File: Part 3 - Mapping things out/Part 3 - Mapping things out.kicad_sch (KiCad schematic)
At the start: 15 parts, among them J1 BUS 1, SW1 RESET, U1 74AHC14, U2 74AHC174

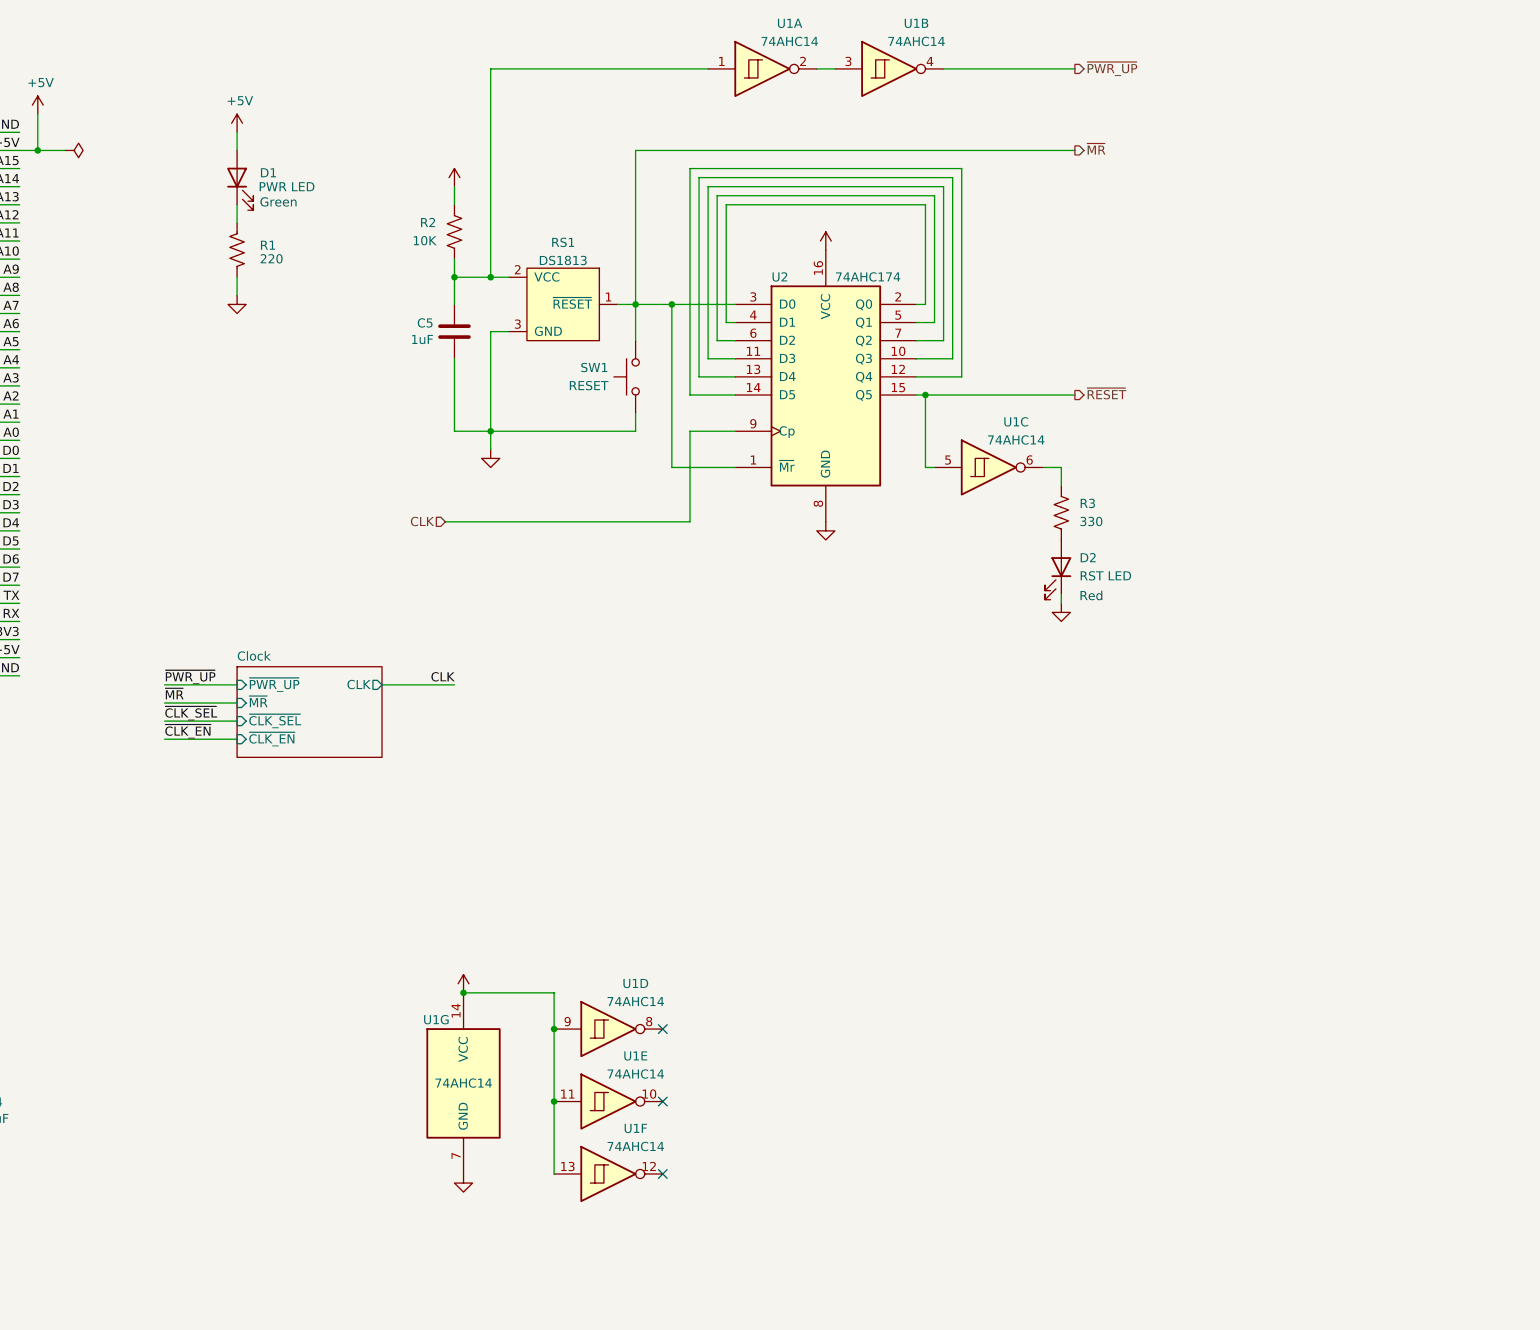
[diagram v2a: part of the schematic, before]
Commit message: Added software selectable speed control
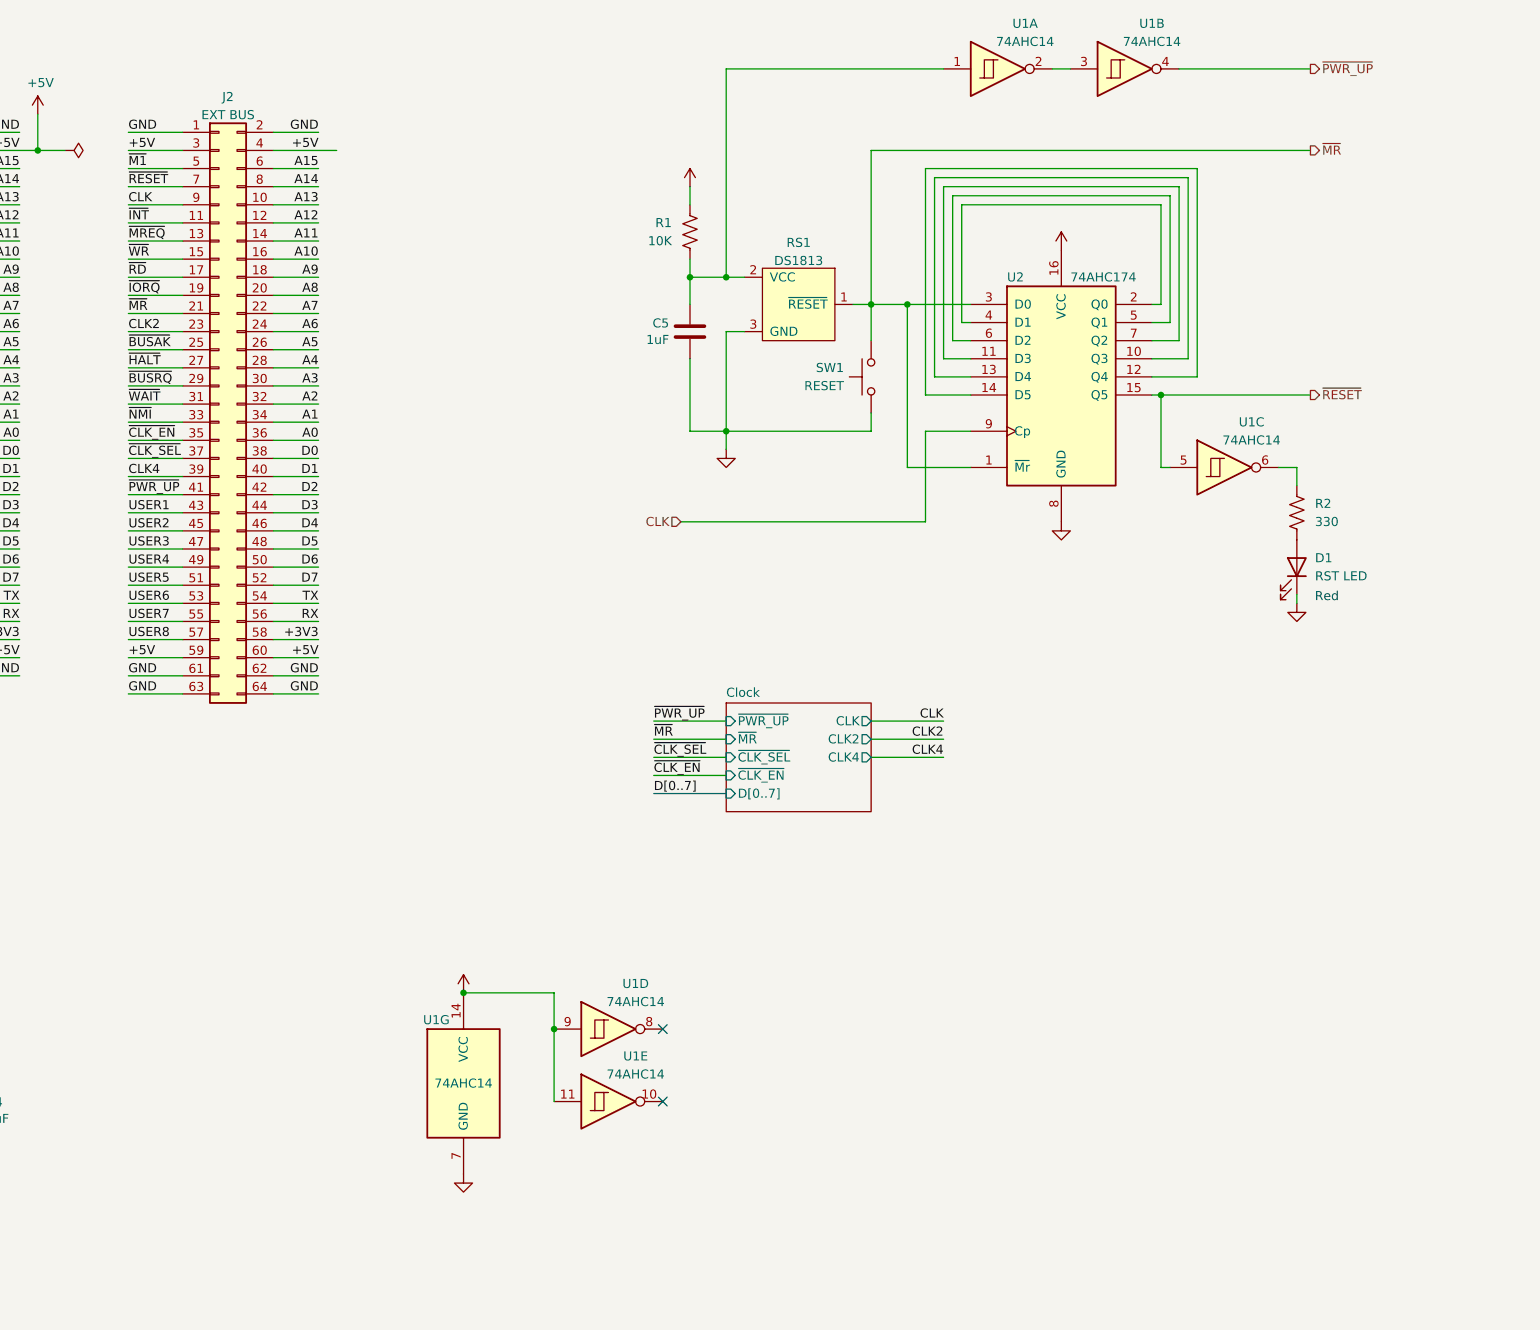
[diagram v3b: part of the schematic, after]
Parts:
- removed D1: PWR LED, LED_THT:LED_D3.0mm, symbol Device:LED
- removed R1: 220, Resistor_THT:R_Axial_DIN0207_L6.3mm_D2.5mm_P10.16mm_Horizontal, symbol Device:R_US
- removed unit 6 of U1
- added J2: EXT BUS, Connector_PinSocket_2.54mm:PinSocket_2x32_P2.54mm_Vertical, symbol Connector_Generic:Conn_02x32_Odd_Even
- SW1: footprint Button_Switch_THT:SW_PUSH-12mm_Wuerth-430476085716 -> Button_Switch_THT:SW_Tactile_SPST_Angled_PTS645Vx58-2LFS
- renumbered D2 to D1, R2 to R1, R3 to R2
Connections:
- net +3V3: now also J2.58 (Pin_58)
- net +5V: now also J2.3 (Pin_3), J2.4 (Pin_4), J2.59 (Pin_59), J2.60 (Pin_60)
- net A0: now also J2.36 (Pin_36)
- net A1: now also J2.34 (Pin_34)
- net A10: now also J2.16 (Pin_16)
- net A11: now also J2.14 (Pin_14)
- net A12: now also J2.12 (Pin_12)
- net A13: now also J2.10 (Pin_10)
- net A14: now also J2.8 (Pin_8)
- net A15: now also J2.6 (Pin_6)
- net A2: now also J2.32 (Pin_32)
- net A3: now also J2.30 (Pin_30)
- net A4: now also J2.28 (Pin_28)
- net A5: now also J2.26 (Pin_26)
- net A6: now also J2.24 (Pin_24)
- net A7: now also J2.22 (Pin_22)
- net A8: now also J2.20 (Pin_20)
- net A9: now also J2.18 (Pin_18)
- net CLK: now also J2.9 (Pin_9)
- net CLK2: now also J2.23 (Pin_23)
- net CLK4: now also J2.39 (Pin_39)
- net D0: now also J2.38 (Pin_38)
- net D1: now also J2.40 (Pin_40)
- net D2: now also J2.42 (Pin_42)
- net D3: now also J2.44 (Pin_44)
- net D4: now also J2.46 (Pin_46)
- net D5: now also J2.48 (Pin_48)
- net D6: now also J2.50 (Pin_50)
- net D7: now also J2.52 (Pin_52)
- net GND: now also J2.1 (Pin_1), J2.2 (Pin_2), J2.61 (Pin_61), J2.62 (Pin_62), J2.63 (Pin_63), J2.64 (Pin_64)
- net RX: now also J2.56 (Pin_56)
- net TX: now also J2.54 (Pin_54)
- net USER1: now also J2.43 (Pin_43)
- net USER2: now also J2.45 (Pin_45)
- net USER3: now also J2.47 (Pin_47)
- net USER4: now also J2.49 (Pin_49)
- net USER5: now also J2.51 (Pin_51)
- net USER6: now also J2.53 (Pin_53)
- net USER7: now also J2.55 (Pin_55)
- net USER8: now also J2.57 (Pin_57)
- net ~{BUSAK}: now also J2.25 (Pin_25)
- net ~{BUSRQ}: now also J2.29 (Pin_29)
- net ~{CLK_EN}: now also J2.35 (Pin_35)
- net ~{CLK_SEL}: now also J2.37 (Pin_37)
- net ~{HALT}: now also J2.27 (Pin_27)
- net ~{INT}: now also J2.11 (Pin_11)
- net ~{IORQ}: now also J2.19 (Pin_19)
- net ~{M1}: now also J2.5 (Pin_5)
- net ~{MREQ}: now also J2.13 (Pin_13)
- net ~{MR}: now also J2.21 (Pin_21)
- net ~{NMI}: now also J2.33 (Pin_33)
- net ~{PWR_UP}: now also J2.41 (Pin_41)
- net ~{RD}: now also J2.17 (Pin_17)
- net ~{RESET}: now also J2.7 (Pin_7)
- net ~{WAIT}: now also J2.31 (Pin_31)
- net ~{WR}: now also J2.15 (Pin_15)
- no-connect marks 3 -> 2
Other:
- sheet Clock ports: added CLK2, CLK4, D[0..7]; removed none
- note removed: "Green"
- company: Frédéric Segard -> Frédéric Segard, aka : Micro Hobbyist
- moved on the sheet: C5, D1, R1, R2, RS1, SW1, U1A, U1B, U1C, U2

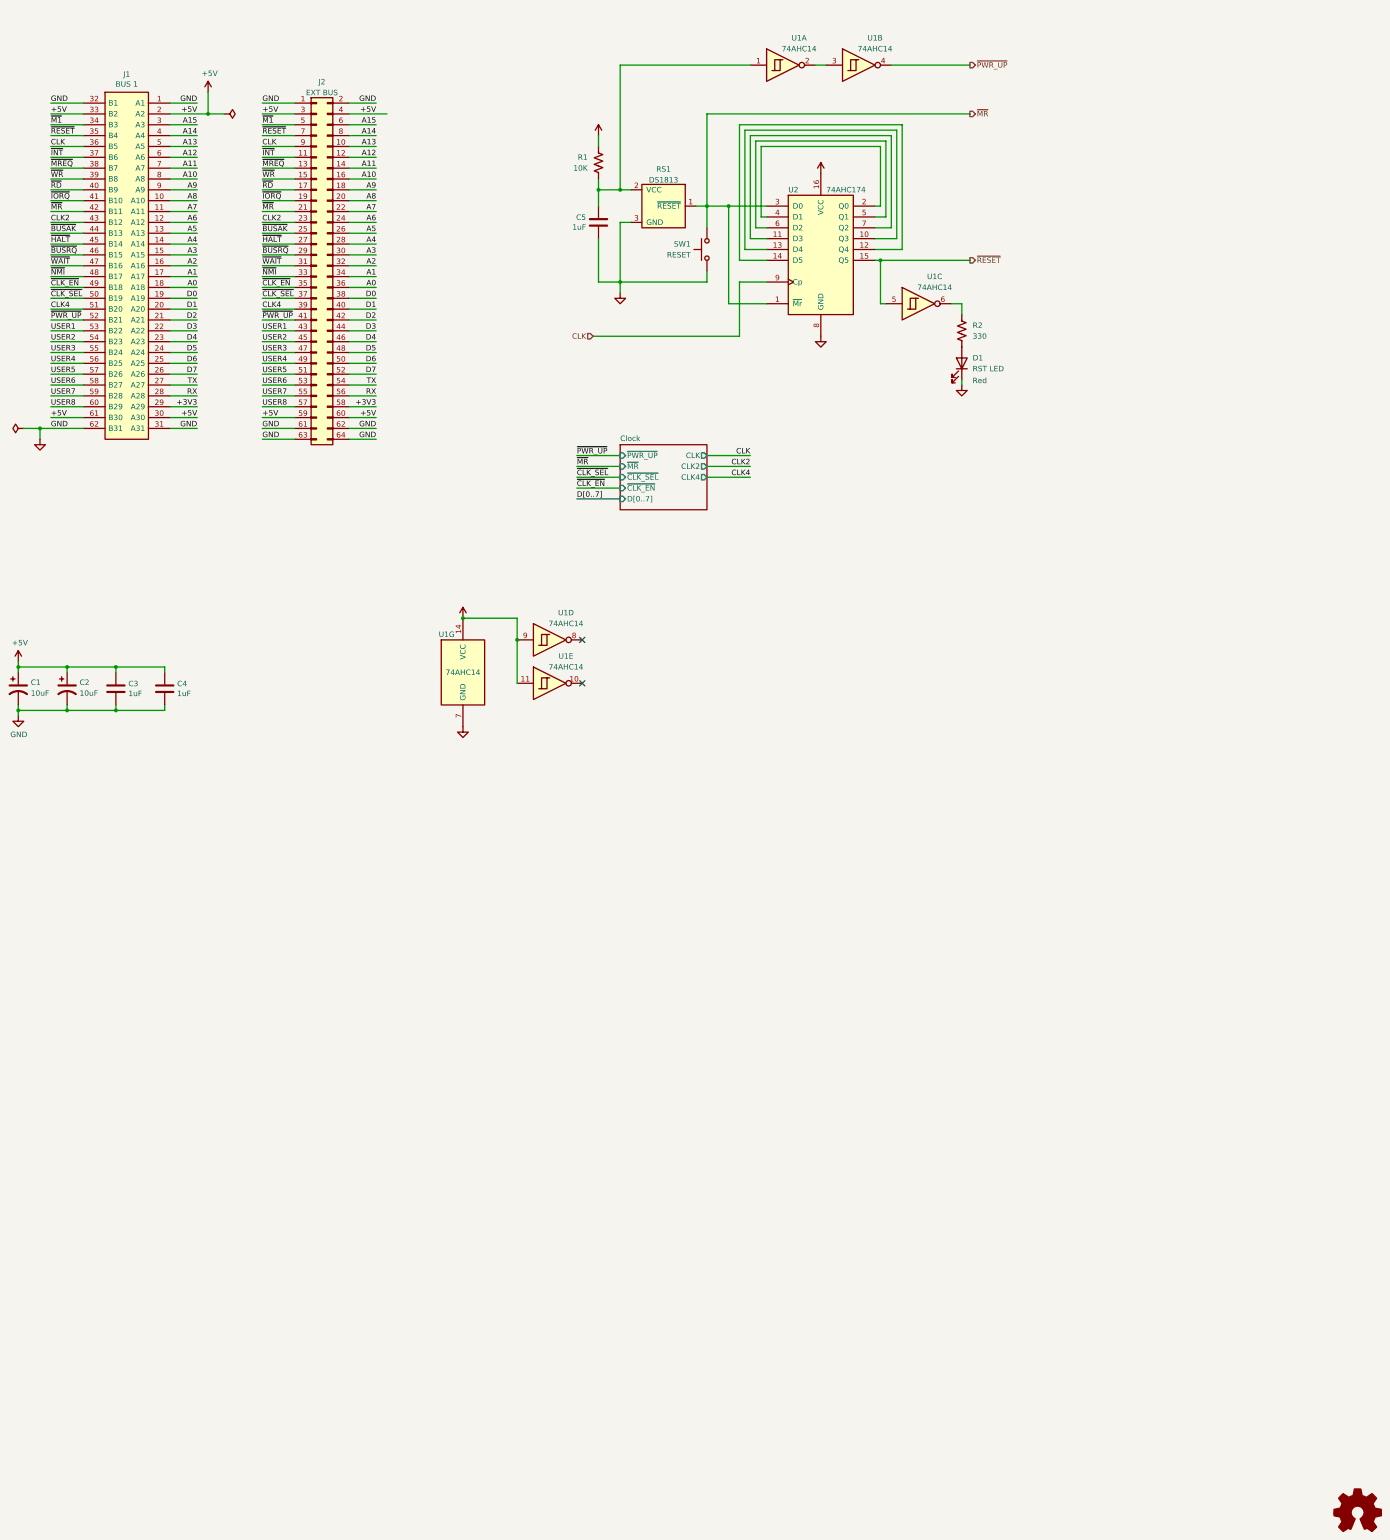
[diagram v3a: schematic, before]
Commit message: Updated clock, and created CPU card
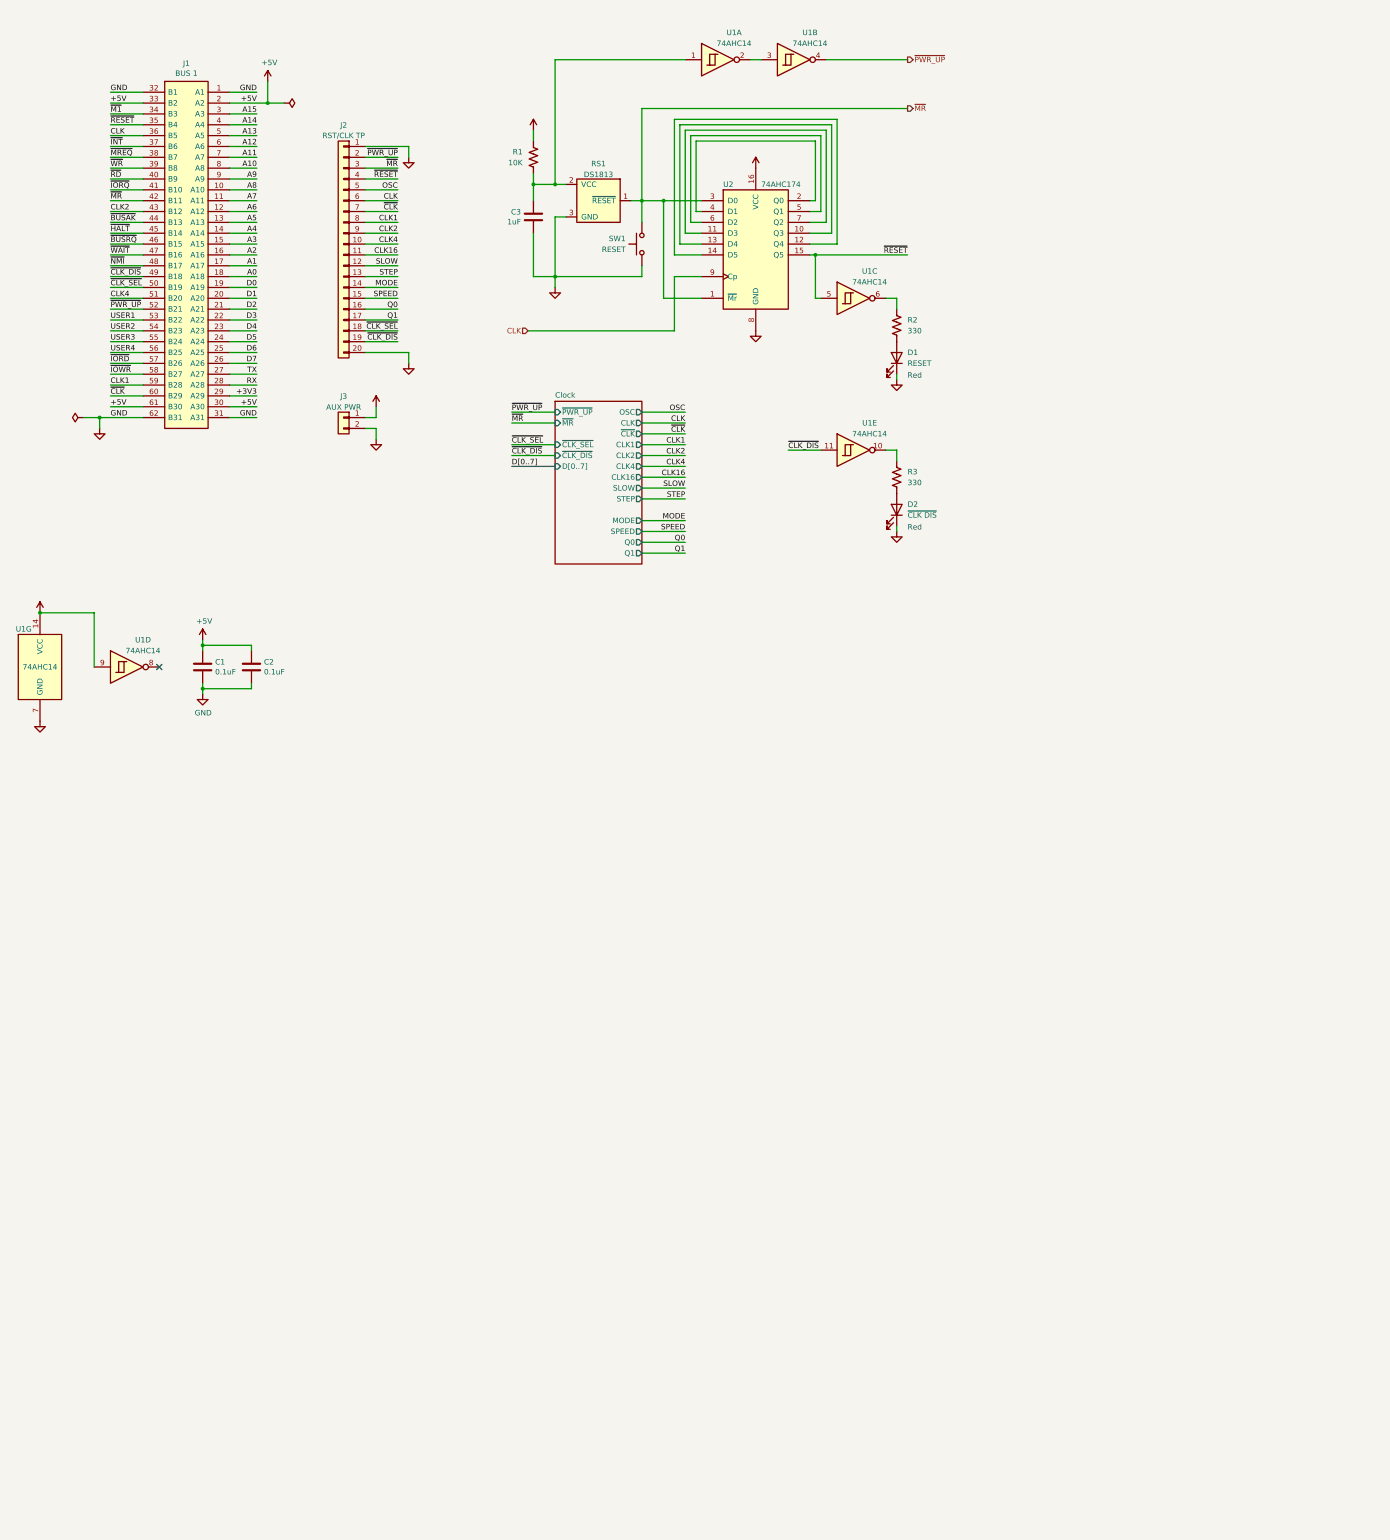
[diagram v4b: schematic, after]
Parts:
- removed C1, C2: 10uF, Capacitor_THT:CP_Radial_D6.3mm_P2.50mm, symbol Device:C_Polarized_US
- removed J2: EXT BUS, Connector_PinSocket_2.54mm:PinSocket_2x32_P2.54mm_Vertical, symbol Connector_Generic:Conn_02x32_Odd_Even
- added D2: ~{CLK DIS}, LED_THT:LED_D3.0mm_Horizontal_O1.27mm_Z2.0mm_Clear, symbol Device:LED
- added J2: RST/CLK TP, Connector_PinSocket_2.54mm:PinSocket_1x20_P2.54mm_Horizontal, symbol Connector_Generic:Conn_01x20
- added J3: AUX PWR, Connector_PinSocket_2.54mm:PinSocket_1x02_P2.54mm_Horizontal, symbol Connector_Generic:Conn_01x02
- added R3: 330, Resistor_THT:R_Axial_DIN0207_L6.3mm_D2.5mm_P10.16mm_Horizontal, symbol Device:R_US
- C1: renamed from C3; value 1uF -> 0.1uF
- C2: renamed from C4; value 1uF -> 0.1uF
- D1: value RST LED -> RESET
- renumbered C5 to C3
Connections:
- net +5V: now also J3.1 (Pin_1); no longer U1.11
- net CLK: now also J2.6 (Pin_6)
- net CLK2: now also J2.9 (Pin_9)
- net CLK4: now also J2.10 (Pin_10)
- net GND: now also D2.1 (K), J2.1 (Pin_1), J2.20 (Pin_20), J3.2 (Pin_2)
- net ~{CLK_SEL}: now also J2.18 (Pin_18)
- net ~{MR}: now also J2.3 (Pin_3)
- net ~{PWR_UP}: now also J2.2 (Pin_2)
- net ~{RESET}: now also J2.4 (Pin_4)
- net at U1.10: now also R3.1
- net USER5 renamed ~{IORD}
- net USER6 renamed ~{IOWR}
- net USER7 renamed CLK1
- net CLK1: now also J2.8 (Pin_8)
- net USER8 renamed ~{CLK}
- net ~{CLK}: now also J2.7 (Pin_7)
- net ~{CLK_EN} renamed ~{CLK_DIS}
- net ~{CLK_DIS}: now also U1.11, J2.19 (Pin_19)
- new net: D2.2 (A), R3.2
- new net CLK16: J2.11 (Pin_11)
- new net MODE: J2.14 (Pin_14)
- new net OSC: J2.5 (Pin_5)
- new net Q0: J2.16 (Pin_16)
- new net Q1: J2.17 (Pin_17)
- new net SLOW: J2.12 (Pin_12)
- new net SPEED: J2.15 (Pin_15)
- new net STEP: J2.13 (Pin_13)
- no-connect marks 2 -> 1
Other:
- sheet Clock ports: added CLK1, CLK16, MODE, OSC, Q0, Q1, SLOW, SPEED, STEP, ~{CLK_DIS}, ~{CLK}; removed ~{CLK_EN}
- company: Frédéric Segard, aka : Micro Hobbyist -> Frédéric Segard
- title: Micro Hobbyist's Z80 Homebrew Project -> Micro Hobbyist's ZedEighty Project
- moved on the sheet: C1, C2, C3, D1, J1, R1, R2, RS1, SW1, U1A, U1B, U1C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
